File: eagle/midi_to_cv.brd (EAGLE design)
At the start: 100 x 80 mm, 46 parts, among them IC1 TL084P, IC2 TL084P, U1 ATMEGA328P_PDIP

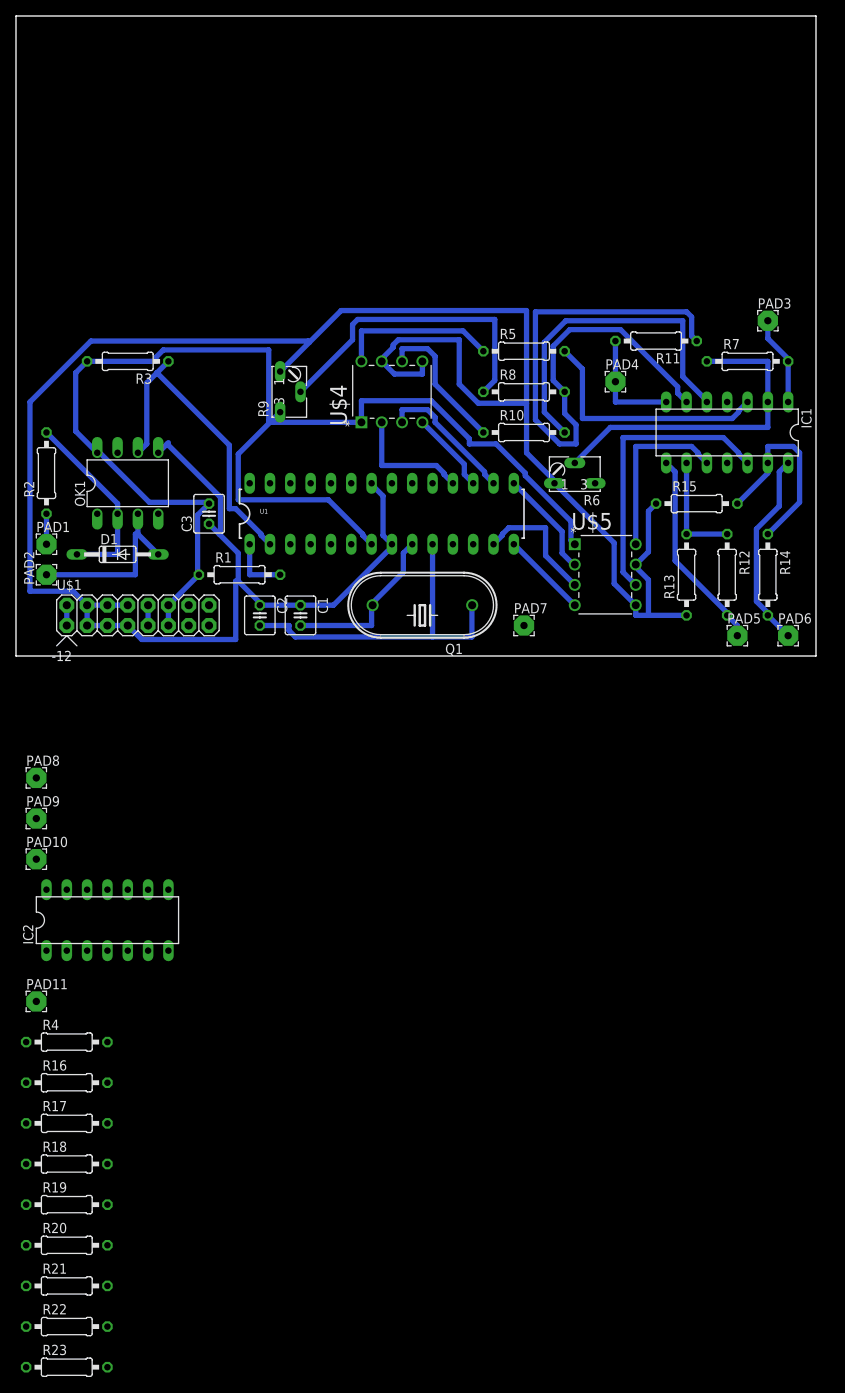
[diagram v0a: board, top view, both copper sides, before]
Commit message: adding four programmable gates outputs
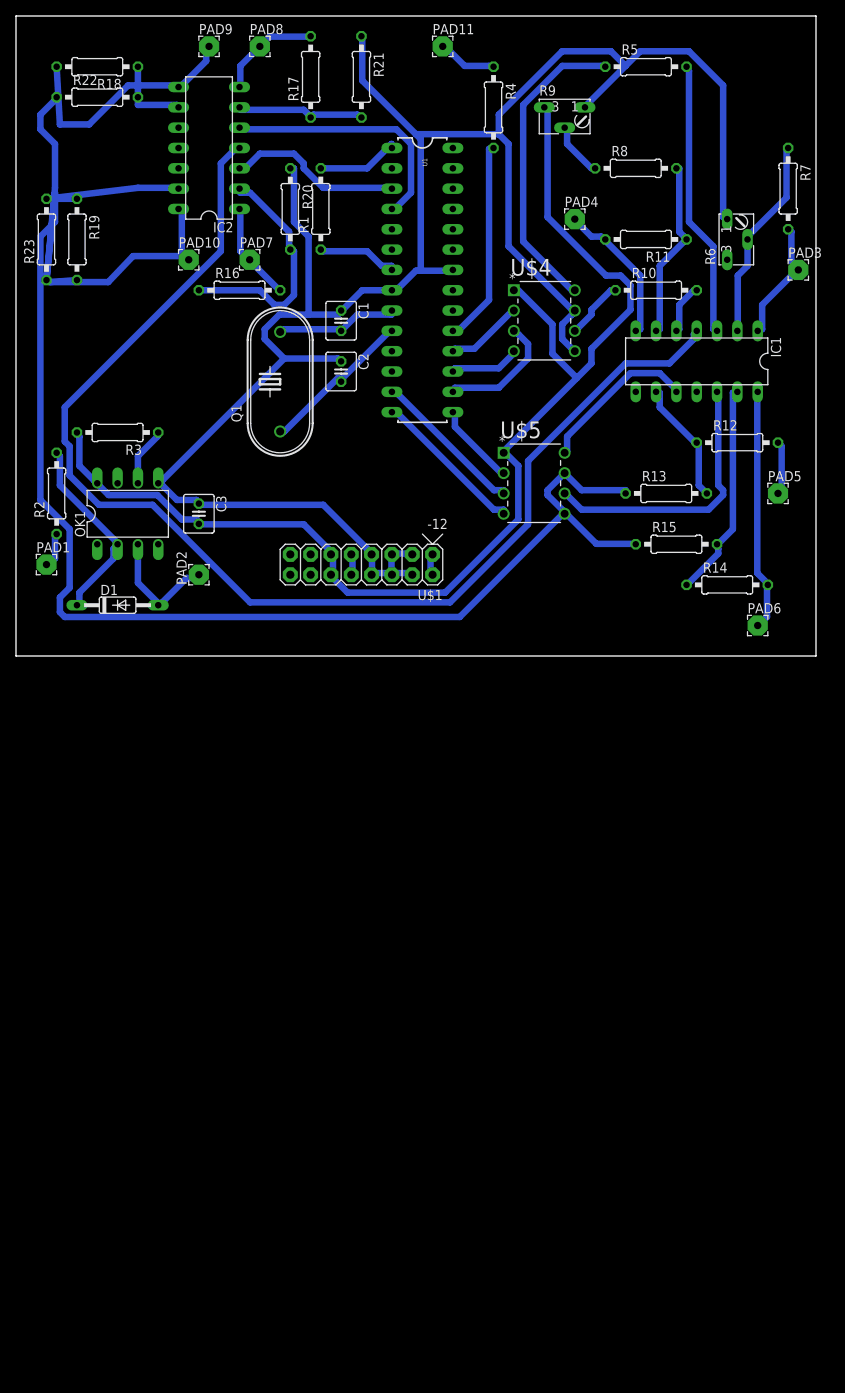
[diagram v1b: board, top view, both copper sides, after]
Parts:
- moved R21 155.6 mm to (43.2, 72.4), turned to 270 degrees
- moved R22 153.7 mm to (10.2, 69.8)
- moved R23 141.0 mm to (3.81, 52.1), turned to 90 degrees
- moved R18 137.2 mm to (10.2, 73.7), turned to 180 degrees
- moved R17 134.3 mm to (36.8, 72.4), turned to 90 degrees
- moved R20 132.5 mm to (34.3, 55.9), turned to 270 degrees
- moved PAD11 129.7 mm to (53.3, 76.2)
- moved R4 128.4 mm to (59.7, 68.6), turned to 270 degrees
- moved R19 120.7 mm to (7.62, 52.1), turned to 270 degrees
- moved R16 101.4 mm to (27.9, 45.7)
- moved PAD9 98.9 mm to (24.1, 76.2)
- moved IC2 97.4 mm to (24.1, 63.5), turned to 90 degrees
- moved PAD8 95.6 mm to (30.5, 76.2)
- moved PAD10 77.3 mm to (21.6, 49.5)
- moved PAD7 57.1 mm to (29.2, 49.5)
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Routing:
- net V+: track 0.00 -> 154.5 mm
- net GND: track 294.6 -> 445.7 mm
- net N$13: track 78.0 -> 22.7 mm
- net N$15: track 42.2 -> 6.40 mm
- net N$30: track 40.8 -> 7.37 mm
- net N$16: track 38.8 -> 6.96 mm
- net N$32: track 0.00 -> 31.6 mm
- net N$37: track 0.00 -> 31.1 mm
- net N$39: track 0.00 -> 30.0 mm
- net N$38: track 0.00 -> 29.5 mm
- net N$10: track 0.00 -> 25.6 mm
- net N$5: track 43.1 -> 19.9 mm
- net N$31: track 0.00 -> 22.0 mm
- net N$40: track 0.00 -> 20.4 mm
- net N$19: track 25.3 -> 6.74 mm
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
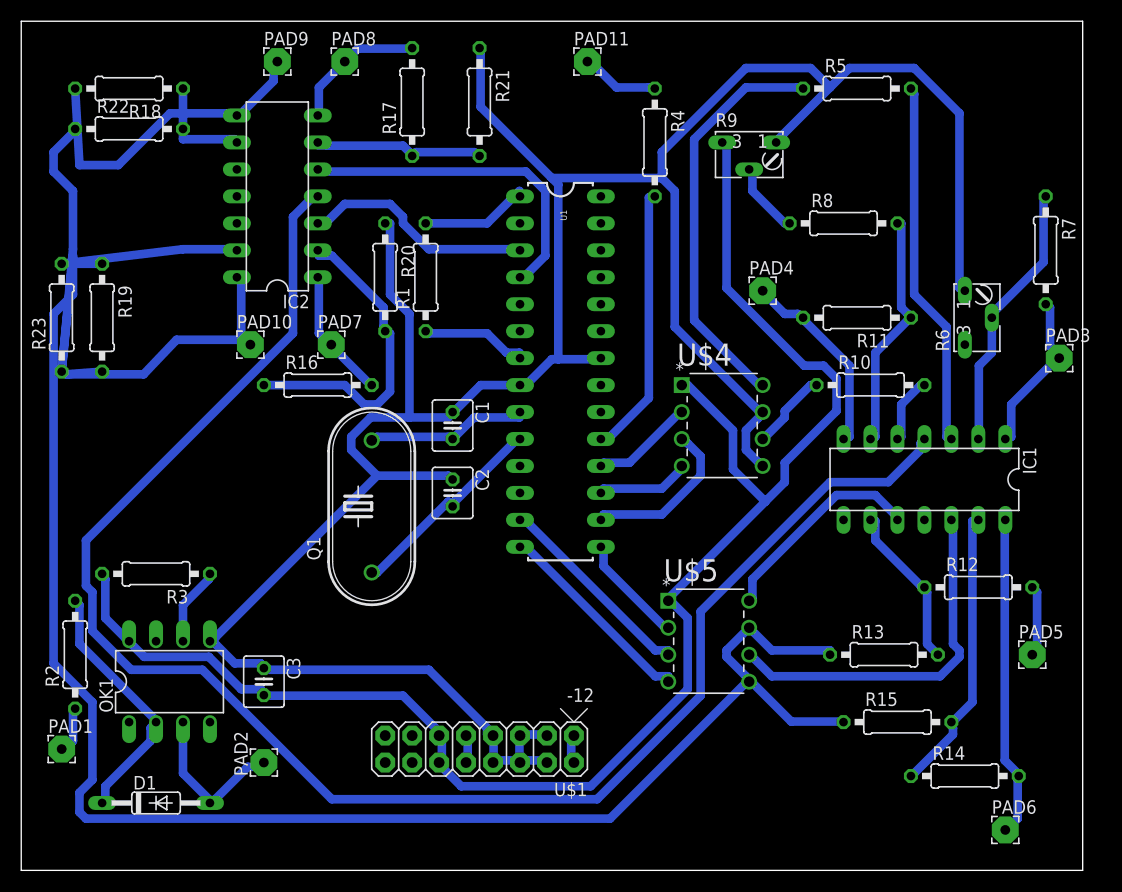
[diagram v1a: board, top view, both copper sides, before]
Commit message: trying to autoroute
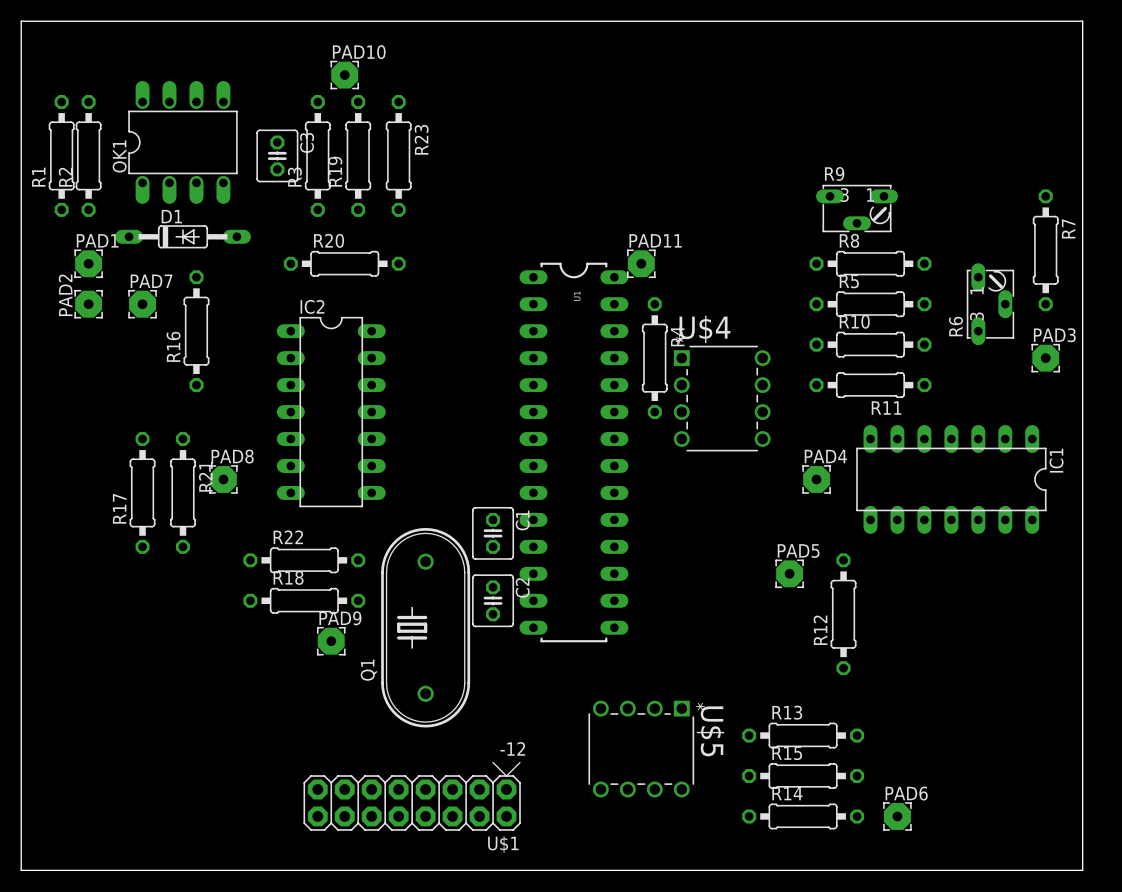
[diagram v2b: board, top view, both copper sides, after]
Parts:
- moved PAD9 54.8 mm to (29.2, 21.6)
- moved D1 53.4 mm to (15.2, 59.7)
- moved R18 51.0 mm to (26.7, 25.4), turned to 0 degrees
- moved OK1 50.8 mm to (15.2, 68.6)
- moved C3 49.5 mm to (24.1, 67.3)
- moved R2 47.0 mm to (6.35, 67.3)
- moved PAD2 46.2 mm to (6.35, 53.3)
- moved R21 46.2 mm to (15.2, 35.6)
- moved PAD1 45.8 mm to (6.35, 57.1)
- moved R17 44.7 mm to (11.4, 35.6)
- moved R22 43.9 mm to (26.7, 29.2)
- moved R3 42.2 mm to (27.9, 67.3), turned to 90 degrees
- moved PAD8 41.0 mm to (19.1, 36.8)
- moved R1 36.1 mm to (3.81, 67.3)
- moved R23 35.2 mm to (35.6, 67.3), turned to 270 degrees
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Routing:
- net GND: track 445.7 -> 0.00 mm
- net +5V: track 160.9 -> 0.00 mm
- net V+: track 154.5 -> 0.00 mm
- net N$2: track 38.3 -> 0.00 mm
- net N$6: track 34.7 -> 0.00 mm
- net N$24: track 34.6 -> 0.00 mm
- net N$32: track 31.6 -> 0.00 mm
- net N$37: track 31.1 -> 0.00 mm
- net N$21: track 30.3 -> 0.00 mm
- net N$39: track 30.0 -> 0.00 mm
- net N$38: track 29.5 -> 0.00 mm
- net N$22: track 27.1 -> 0.00 mm
- net N$10: track 25.6 -> 0.00 mm
- net N$12: track 25.5 -> 0.00 mm
- net N$7: track 24.4 -> 0.00 mm
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
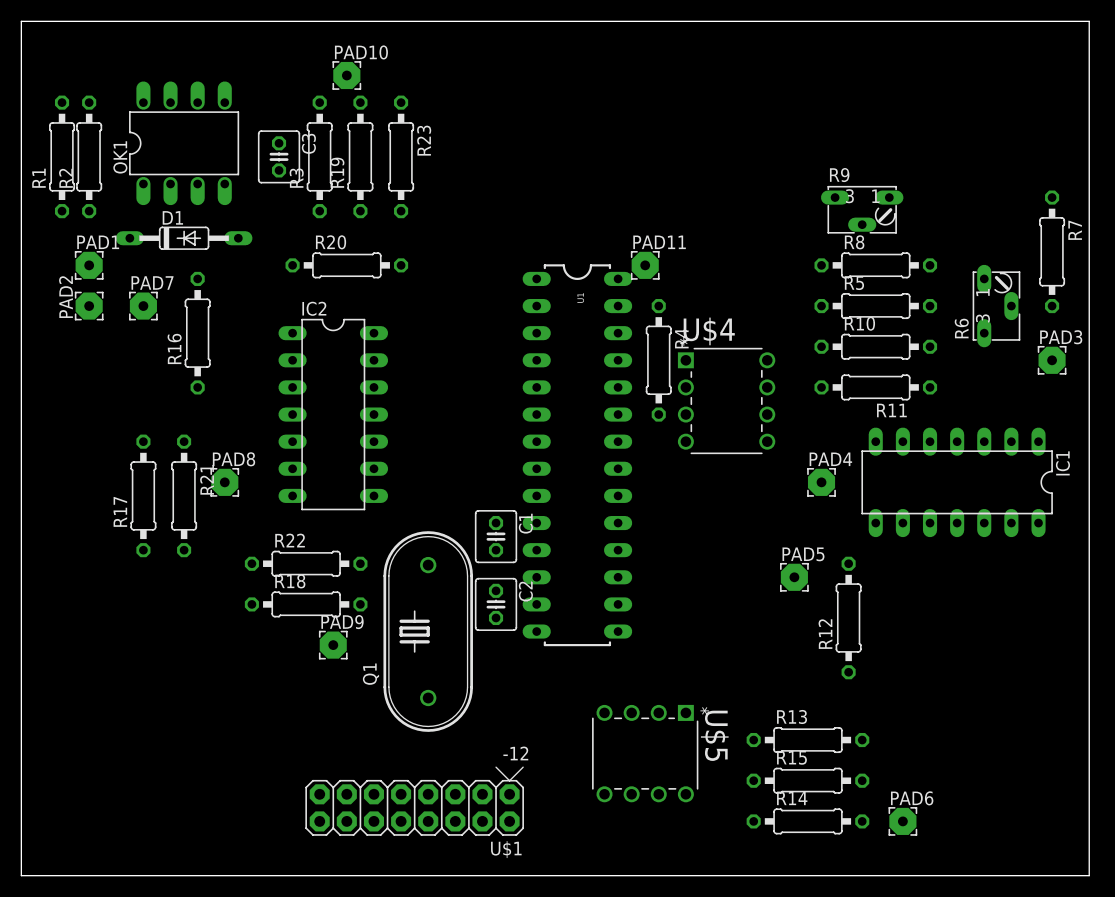
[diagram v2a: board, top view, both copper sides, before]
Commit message: power to the op amps
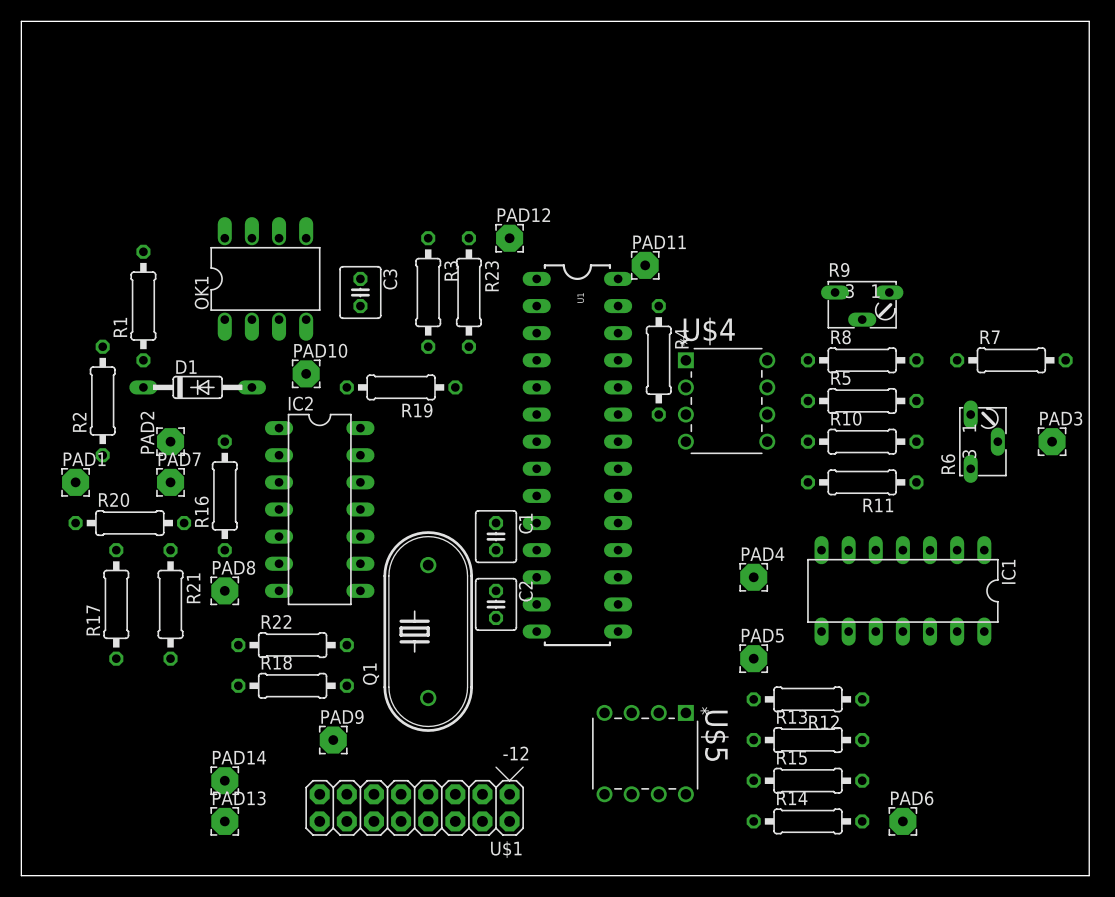
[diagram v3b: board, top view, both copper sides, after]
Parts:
- added PAD12, PAD13: reset, wirepad:2,54/0,9
- added PAD14: gate LED, wirepad:2,54/0,9
- moved R20 31.5 mm to (10.2, 33.0)
- moved PAD10 28.2 mm to (26.7, 47.0)
- moved R2 22.9 mm to (7.62, 44.5)
- moved R19 21.9 mm to (35.6, 45.7), turned to 180 degrees
- moved PAD1 20.4 mm to (5.08, 36.8)
- moved PAD7 16.7 mm to (14.0, 36.8)
- moved R3 16.3 mm to (38.1, 54.6), turned to 270 degrees
- moved R1 15.9 mm to (11.4, 53.3)
- moved R16 15.5 mm to (19.1, 35.6)
- moved C3 14.8 mm to (31.8, 54.6)
- moved PAD2 14.8 mm to (14.0, 40.6)
- moved OK1 14.8 mm to (22.9, 55.9)
- moved R23 14.2 mm to (41.9, 54.6)
- moved D1 14.0 mm to (16.5, 45.7)
- moved R6 12.8 mm to (88.9, 40.6)
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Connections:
- removed net V+: IC1.4, IC2.4
- removed net V-: IC1.11, IC2.11
- net +12V: now also IC1.4, IC2.4
- net -12V: now also IC1.11, IC2.11
- net GND: now also PAD13.1, PAD14.1
- net N$1: now also PAD12.1

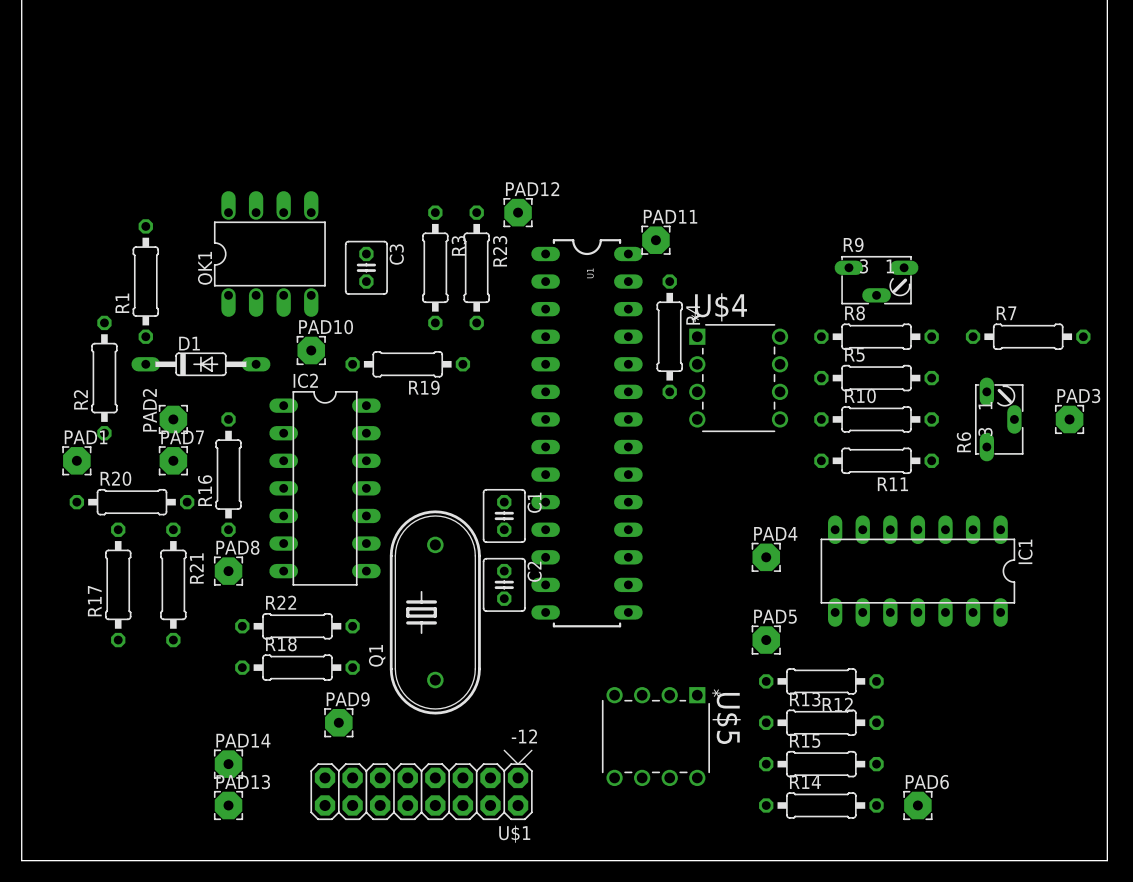
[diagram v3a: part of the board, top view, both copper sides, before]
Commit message: toward a routing for the gates
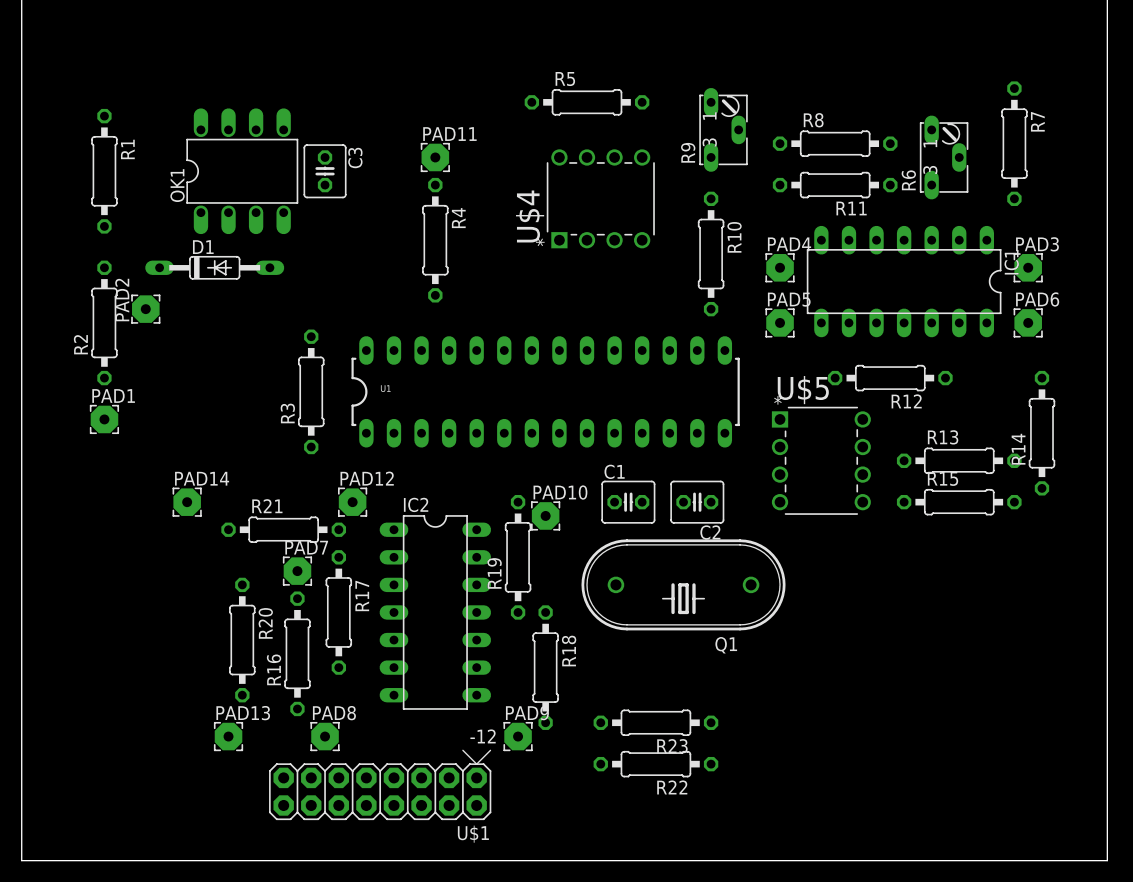
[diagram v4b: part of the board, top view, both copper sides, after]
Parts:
- moved PAD6 45.6 mm to (92.7, 49.5)
- moved R23 45.0 mm to (58.4, 12.7), turned to 180 degrees
- moved R14 39.9 mm to (94.0, 39.4), turned to 90 degrees
- moved R5 36.8 mm to (52.1, 69.8)
- moved R22 35.4 mm to (58.4, 8.89), turned to 180 degrees
- moved U$5 34.2 mm to (77.5, 33.0), turned to 0 degrees
- moved PAD12 30.7 mm to (30.5, 33.0)
- moved PAD5 29.2 mm to (69.8, 49.5)
- moved R12 28.7 mm to (80.0, 44.5)
- moved R15 27.3 mm to (86.4, 33.0)
- moved R13 27.3 mm to (86.4, 36.8)
- moved U$4 27.3 mm to (57.1, 64.8), turned to 90 degrees
- moved IC1 26.7 mm to (81.3, 53.3)
- moved PAD4 26.7 mm to (69.8, 54.6)
- moved PAD10 26.4 mm to (48.3, 31.8)
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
